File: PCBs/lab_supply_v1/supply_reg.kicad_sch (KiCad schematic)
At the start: 48 parts, among them Q1 Q_NPN_BEC, Q2 Q_NPN_BEC, Q3 Q_NPN_BEC, U10 LM334Z, U16 NCS20072D, U3 LT3080xMS8E, U4 LT3080xMS8E, U5 LT3080xMS8E, U6 LT3080xMS8E, U7 LT3080xMS8E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

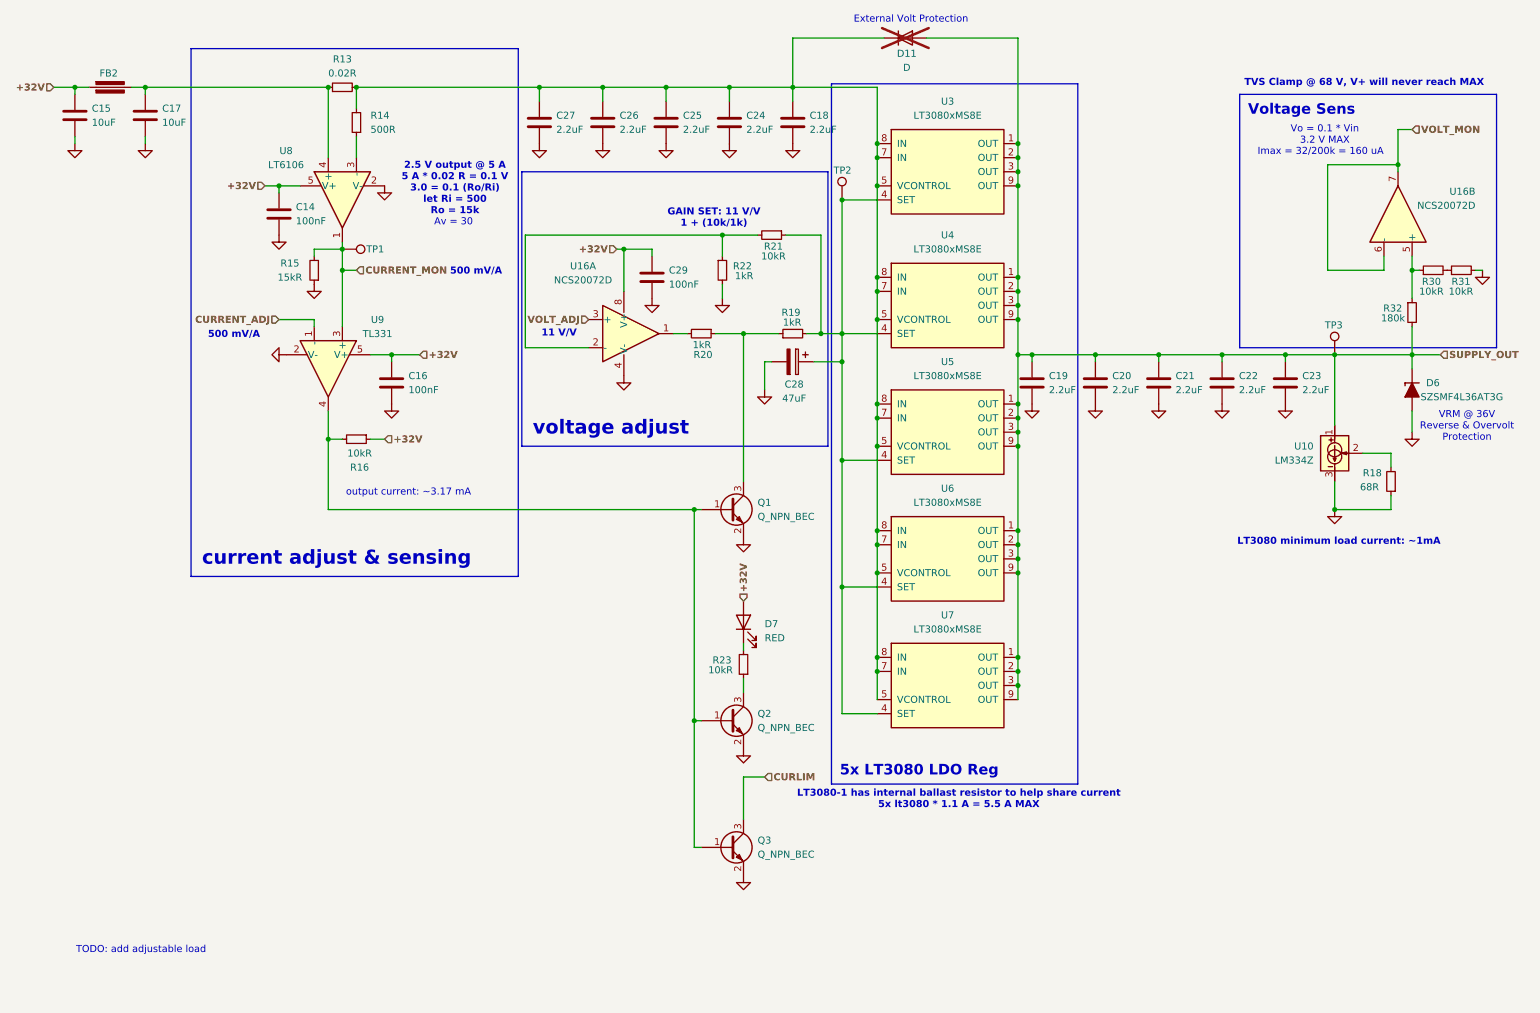
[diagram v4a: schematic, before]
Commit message: Updated PCB added current sense buffer added ADC/DAC for current/voltage sensing added ACDC converter bypass made optimal supply voltage 36 V @ 5 A
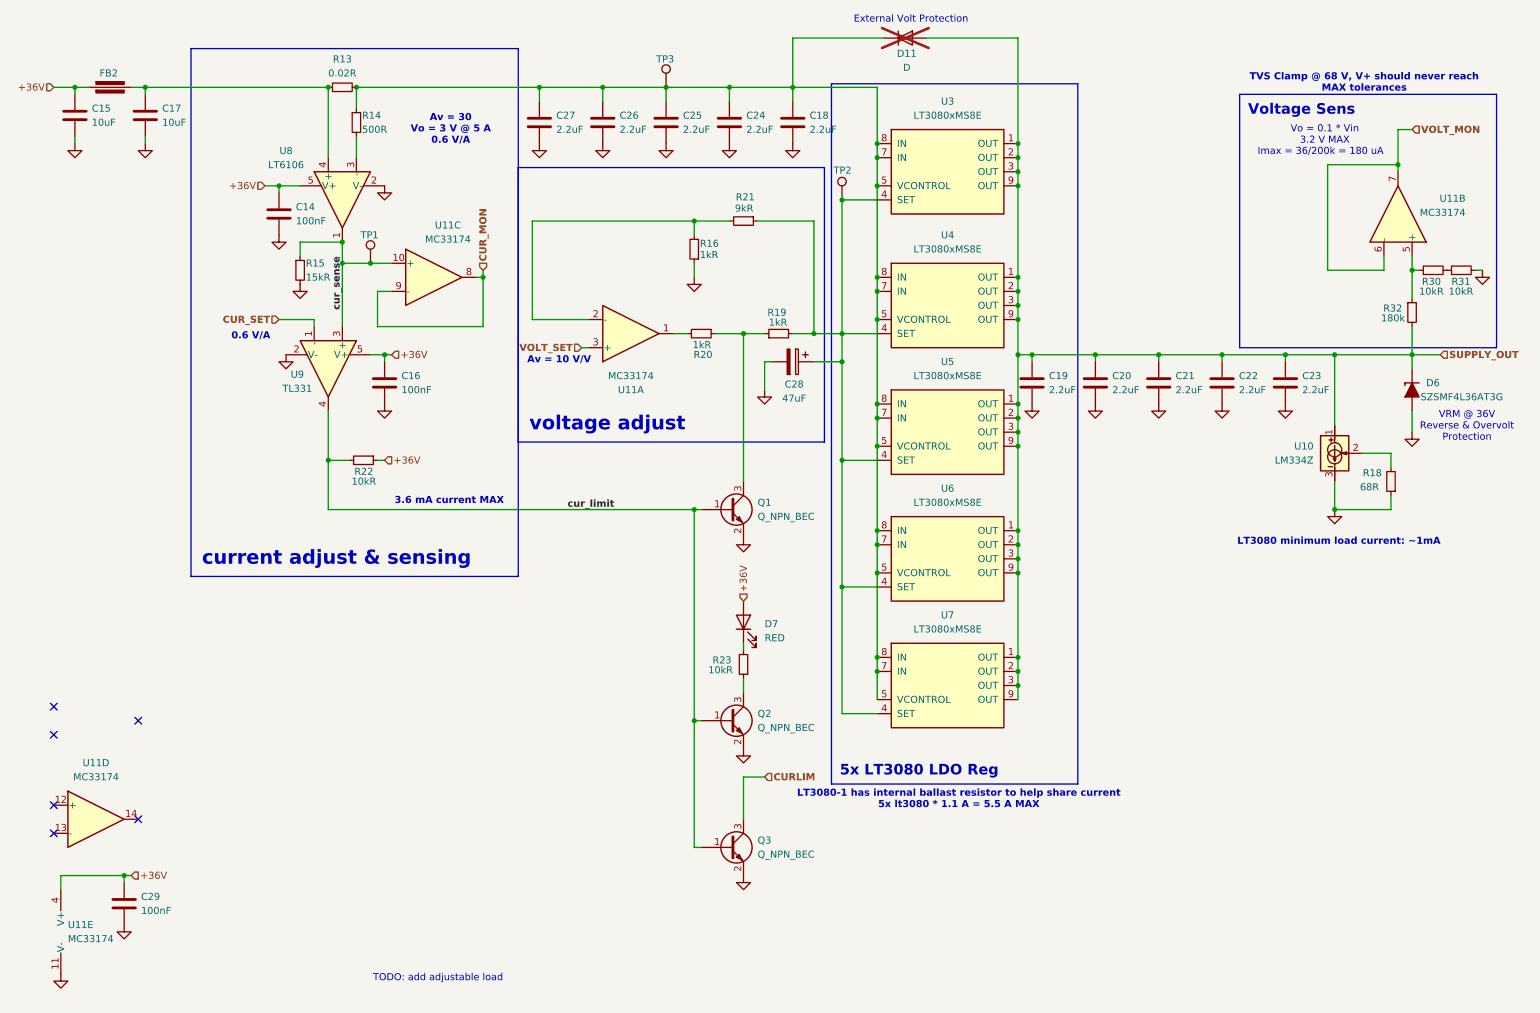
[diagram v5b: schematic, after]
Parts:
- removed U16: NCS20072D, Package_SO:SOIC-8_3.9x4.9mm_P1.27mm, symbol Amplifier_Operational:NCS20072D
- added U11: MC33174, symbol Amplifier_Operational:MC33174
- R16: value 10kR -> 1kR
- R21: value 10kR -> 9kR
- R22: value 1kR -> 10kR
- TP1: value current_sense -> TestPoint
- TP3: value voltage_set -> TestPoint
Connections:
- net GND: now also R15.2, R16.1, U11.11 (V-); no longer R15.1, R22.2
- net SUPPLY_OUT: no longer TP3.1
- net VOLT_MON: now also U11.6 (-), U11.7
- net cur_limit: now reaches Q1.1 (B), Q2.1 (B), Q3.1 (B), U9.4
- net cur_limit: now also R22.2; no longer R16.2
- net at R20.2: now also U11.1
- net at R21.2: now also R16.2, U11.2 (-); no longer R22.1
- net at C18.1, C24.1, C25.1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: now also R14.1, TP3.1; no longer R14.2
- net at R30.1, R32.1: now also U11.5 (+)
- net at U8.3 (-): now also R14.2; no longer R14.1
- net +32V renamed +36V
- net +36V: now also R22.1, U11.4 (V+); no longer R16.1
- net CURRENT_ADJ renamed CUR_SET
- net CURRENT_MON renamed cur_sense
- net cur_sense: now also R15.1, U11.10 (+); no longer R15.2
- new net CUR_MON: U11.8, U11.9 (-)
- new net VOLT_SET: U11.3 (+)
- no-connect marks 0 -> 6
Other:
- note added: "0.6 V/A"
- note added: "3.6 mA current MAX"
- note added: "Av = 10 V/V"
- note added: "Av = 30 Vo = 3 V @ 5 A 0.6 V/A"
- note added: "Imax = 36/200k = 180 uA"
- note added: "TVS Clamp @ 68 V, V+ should never reach MAX tolerances"
- note removed: "11 V/V"
- note removed: "2.5 V output @ 5 A 5 A * 0.02 R = 0.1 V 3.0 = 0.1 (Ro/Ri) let Ri = 500 Ro = 15k"
- note removed: "500 mV/A"
- note removed: "Av = 30"
- note removed: "GAIN SET: 11 V/V 1 + (10k/1k)"
- note removed: "Imax = 32/200k = 160 uA"
- note removed: "TVS Clamp @ 68 V, V+ will never reach MAX"
- note removed: "output current: ~3.17 mA"
- moved on the sheet: R19

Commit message: Updated PCB began dynamic load work
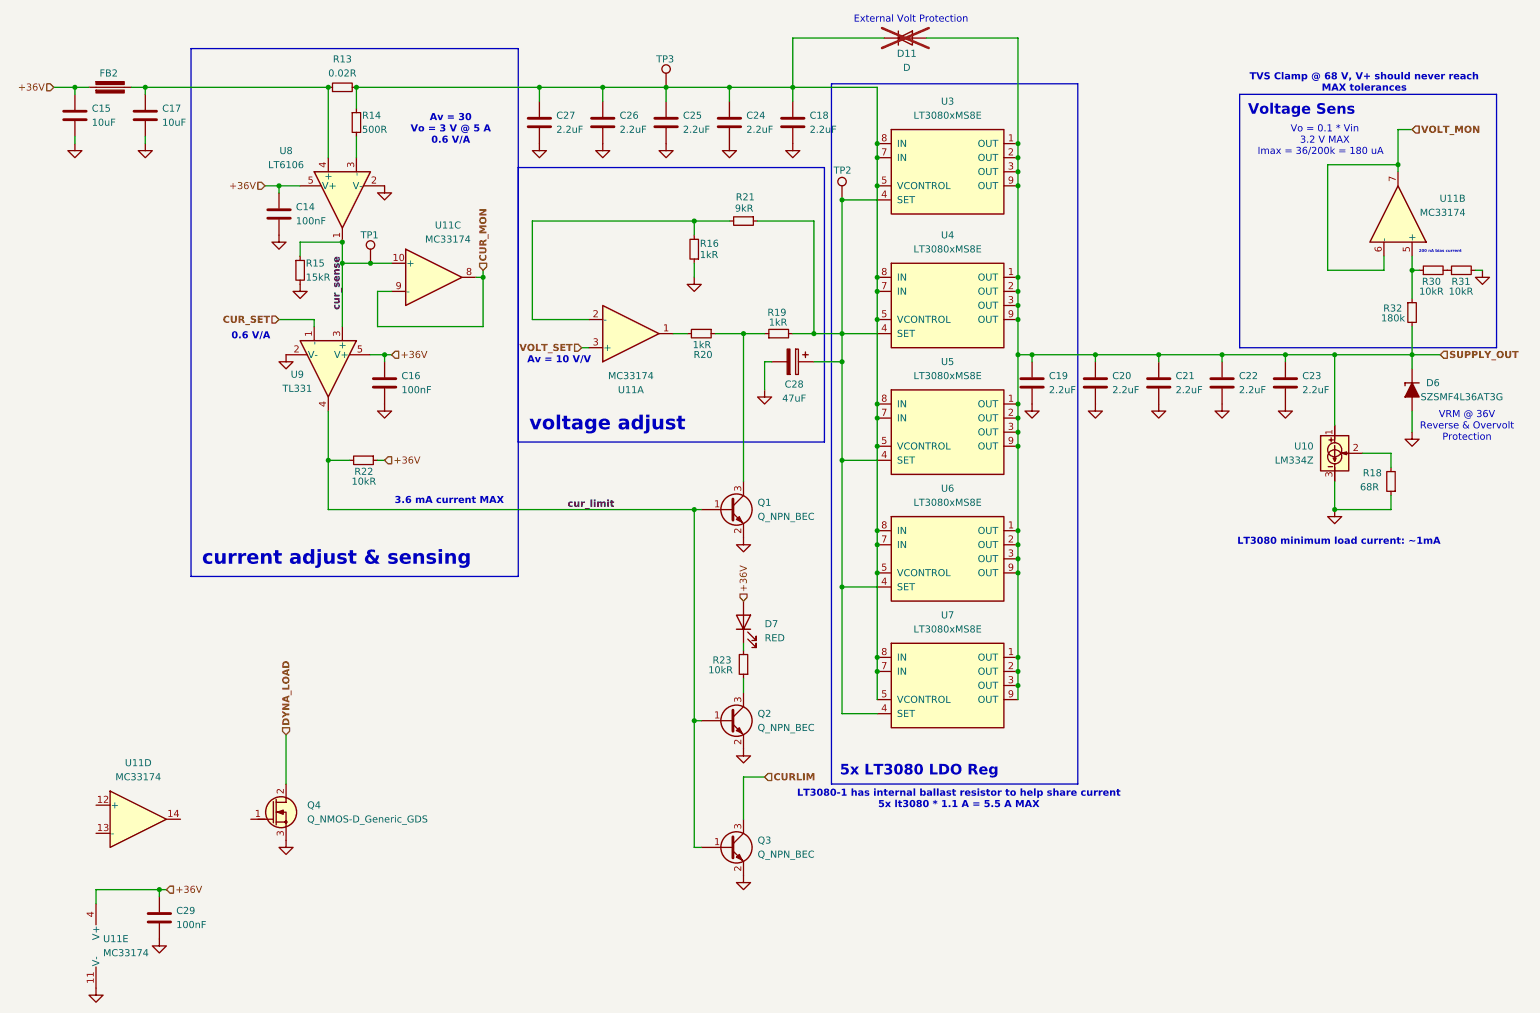
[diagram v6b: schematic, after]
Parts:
- added Q4: Q_NMOS-D_Generic_GDS, symbol PCM_Transistor_MOSFET_AKL:Q_NMOS-D_Generic_GDS
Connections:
- net GND: now also Q4.3 (S)
- new net DYNA_LOAD: Q4.2 (D)
- no-connect marks 6 -> 0
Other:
- note added: "200 nA bias current"
- note removed: "TODO: add adjustable load"
- moved on the sheet: C29, U11E

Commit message: Changed MCU to ESP32 WROOM module Added constant current source (3.3 A max, 150 W)
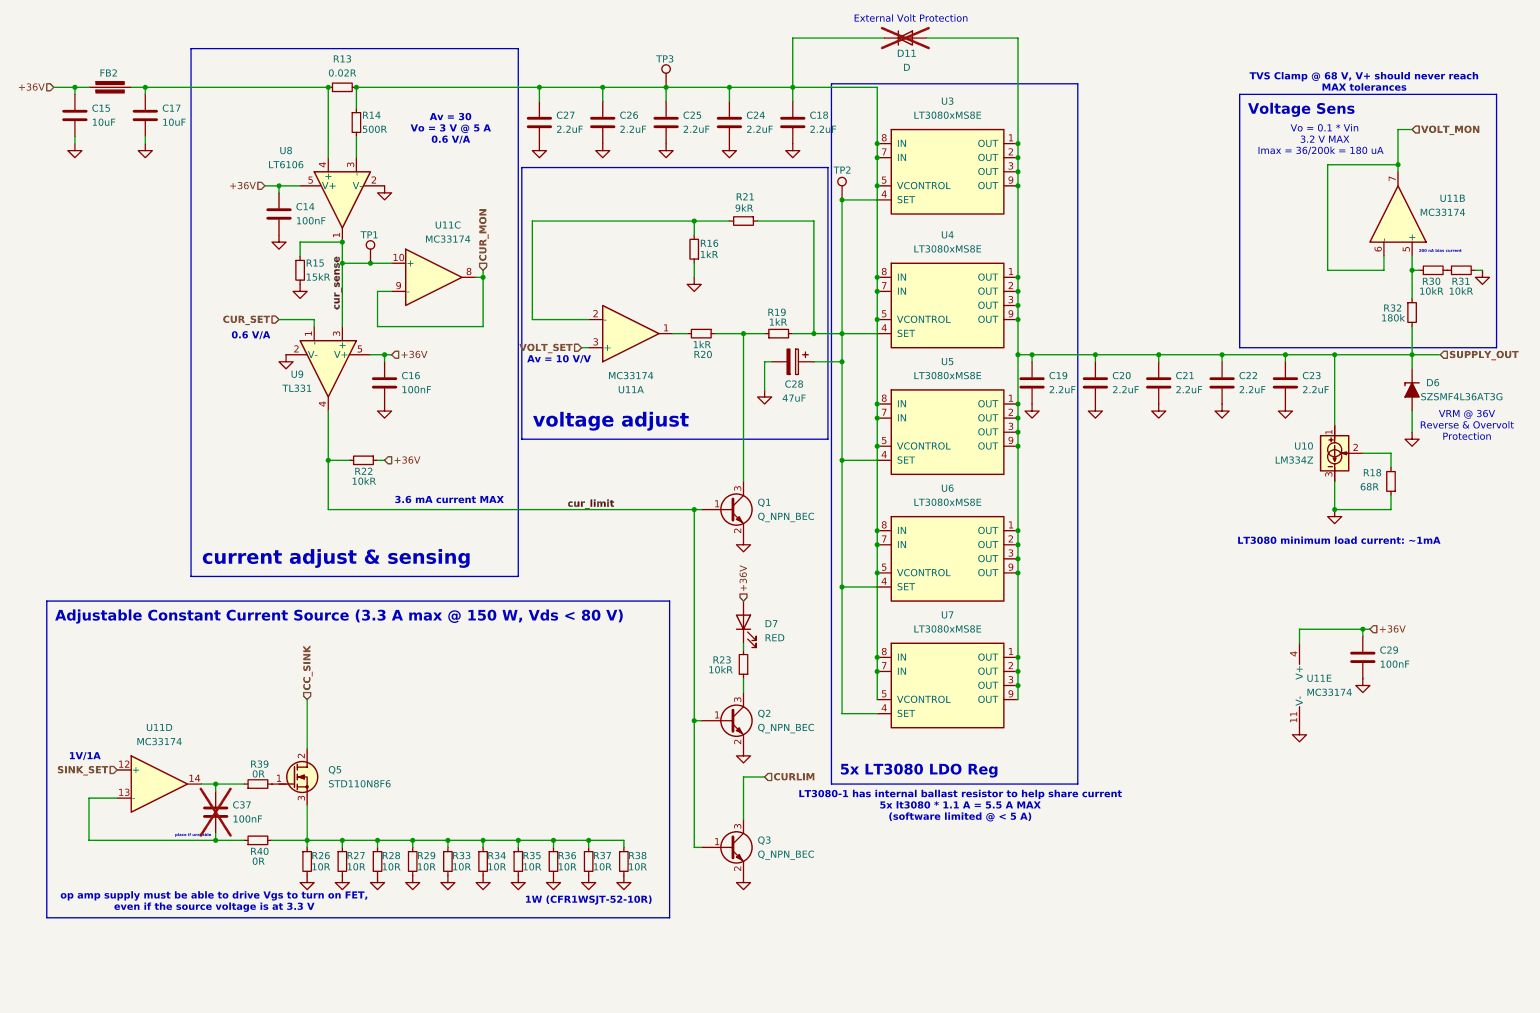
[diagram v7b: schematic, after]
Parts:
- removed Q4: Q_NMOS-D_Generic_GDS, symbol PCM_Transistor_MOSFET_AKL:Q_NMOS-D_Generic_GDS
- added C37: 100nF, symbol Device:C
- added Q5: STD110N8F6, Package_TO_SOT_SMD_AKL:TO-252-2, symbol PCM_Transistor_MOSFET_AKL:STD11NM60ND
- added R26, R27, R28, R29, R33, R34, R35, R36, R37, R38: 10R, symbol Device:R_Small
- added R39, R40: 0R, symbol Device:R_Small
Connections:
- net GND: now also R26.2, R27.2, R28.2, R29.2, R33.2, R34.2, R35.2, R36.2, R37.2, R38.2
- net SINK_SET: now reaches U11.12 (+)
- net at U11.13 (-): now also C37.2, R40.1
- net at U11.14: now also C37.1, R39.1
- new net: Q5.3 (S), R26.1, R27.1, R28.1, R29.1, R33.1, R34.1, R35.1, R36.1, R37.1, R38.1, R40.2
- new net: Q5.1 (G), R39.2
- new net CC_SINK: Q5.2 (D)
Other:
- note added: "1V/1A"
- note added: "1W (CFR1WSJT-52-10R)"
- note added: "LT3080-1 has internal ballast resistor to help share current 5x lt3080 * 1.1 A = 5.5 A MAX (software limited @ < 5 A)"
- note added: "op amp supply must be able to drive Vgs to turn on FET, even if the source voltage is at 3.3 V"
- note added: "place if unstable"
- note removed: "LT3080-1 has internal ballast resistor to help share current 5x lt3080 * 1.1 A = 5.5 A MAX"
- moved on the sheet: C29, U11D, U11E

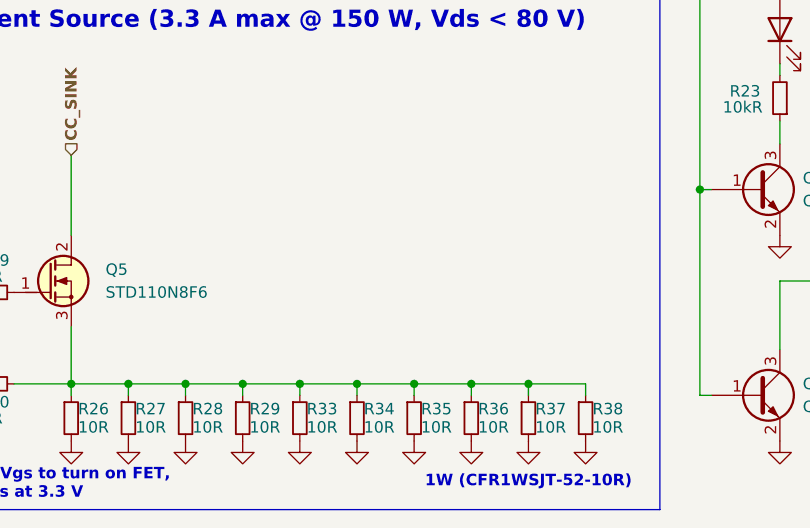
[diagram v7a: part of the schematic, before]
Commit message: added more info to CC sink updated ESP module to fit HiLetgo's ESP32-WROOM
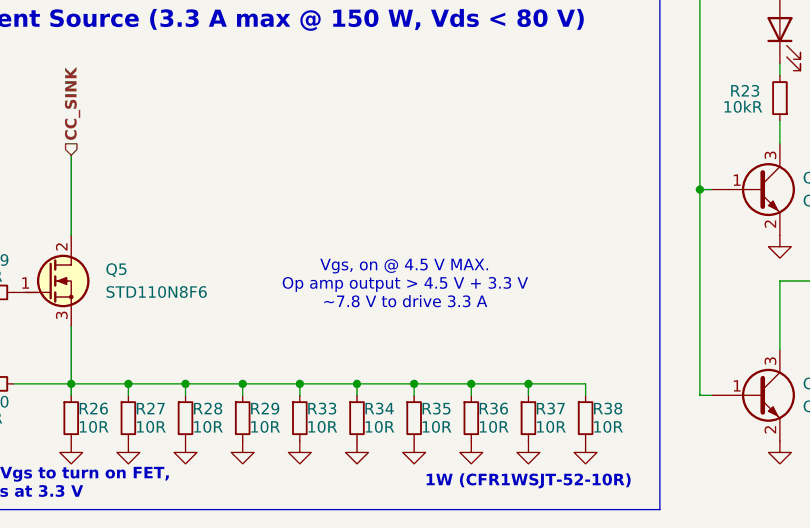
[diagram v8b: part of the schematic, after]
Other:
- note added: "Vgs, on @ 4.5 V MAX. Op amp output > 4.5 V + 3.3 V ~7.8 V to drive 3.3 A"
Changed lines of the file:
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@@
+		)
+	)
+	(text "Vgs, on @ 4.5 V MAX. \nOp amp output > 4.5 V + 3.3 V\n~7.8 V to drive 3.3 A"
+		(exclude_from_sim no)
+		(at 103.124 151.638 0)
+		(effects
+			(font
+				(size 1.27 1.27)
+			)
 		)
 	)
